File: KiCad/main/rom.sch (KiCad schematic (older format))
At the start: 2 parts, among them U8 27C512, U9 27C512

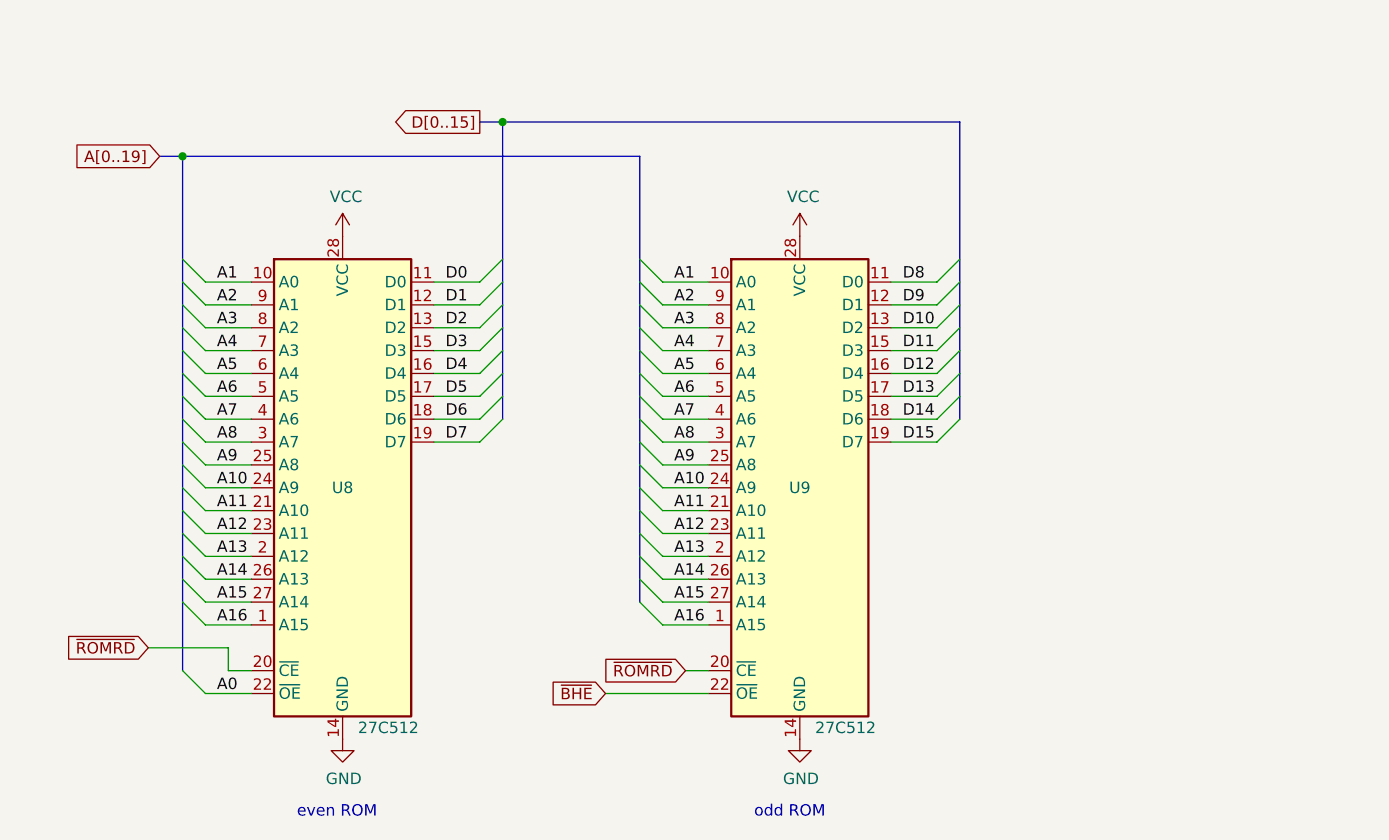
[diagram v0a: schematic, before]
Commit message: Updated KiCad VGA board and main board.
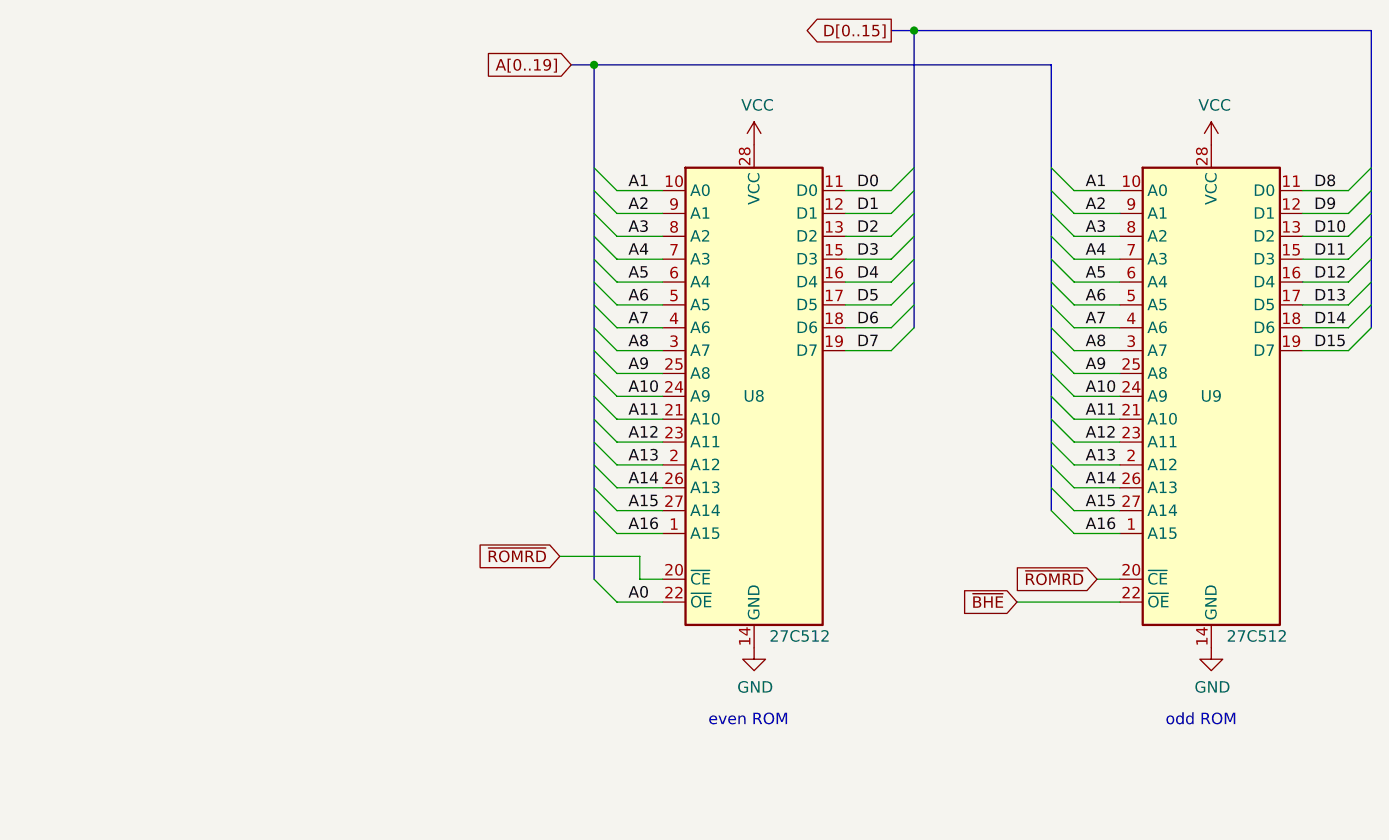
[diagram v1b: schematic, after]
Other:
- moved on the sheet: U8, U9
